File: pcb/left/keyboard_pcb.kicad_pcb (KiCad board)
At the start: 2 copper layers, 138.8 x 89.9 mm, 36 parts, among them J1 TRRS, K00 KEYSW, K01 KEYSW, K02 KEYSW, K03 KEYSW, K04 KEYSW, K05 KEYSW, K10 KEYSW, K11 KEYSW, K12 KEYSW, K13 KEYSW, K14 KEYSW, K15 KEYSW, K20 KEYSW, K21 KEYSW, K22 KEYSW, K23 KEYSW, K24 KEYSW, K25 KEYSW, K30 KEYSW, K31 KEYSW, K32 KEYSW, U2 Pico

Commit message: Fix mounting holes
There were two H1s and three H4s! Add H5–7 and assign M2 mounting hole from KiCad library (no visible change noticed when updating on PCB).
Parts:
- renumbered H4 to H5, H4 to H6, H1 to H7
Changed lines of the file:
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@@
     (property "Sheetname" "")
     (attr exclude_from_pos_files)
-    (fp_text reference "H4" (at 0 -3.2) (layer "F.SilkS") hide
+    (fp_text reference "H5" (at 0 -3.2) (layer "F.SilkS") hide
         (effects (font (size 1 1) (thickness 0.15)))
     )
@@
     (property "Sheetname" "")
     (attr exclude_from_pos_files)
-    (fp_text reference "H4" (at 0 -3.2) (layer "F.SilkS") hide
+    (fp_text reference "H6" (at 0 -3.2) (layer "F.SilkS") hide
         (effects (font (size 1 1) (thickness 0.15)))
     )
@@
     (property "Sheetname" "")
     (attr exclude_from_pos_files)
-    (fp_text reference "H1" (at 0 -3.2) (layer "F.SilkS") hide
-        (effects (font (size 1 1) (thickness 0.15)))
-    )
+    (fp_text reference "H7" (at 0 -3.2) (layer "F.SilkS") hide
+        (effects (font (size 1 1) (thickness 0.15)))
+    )

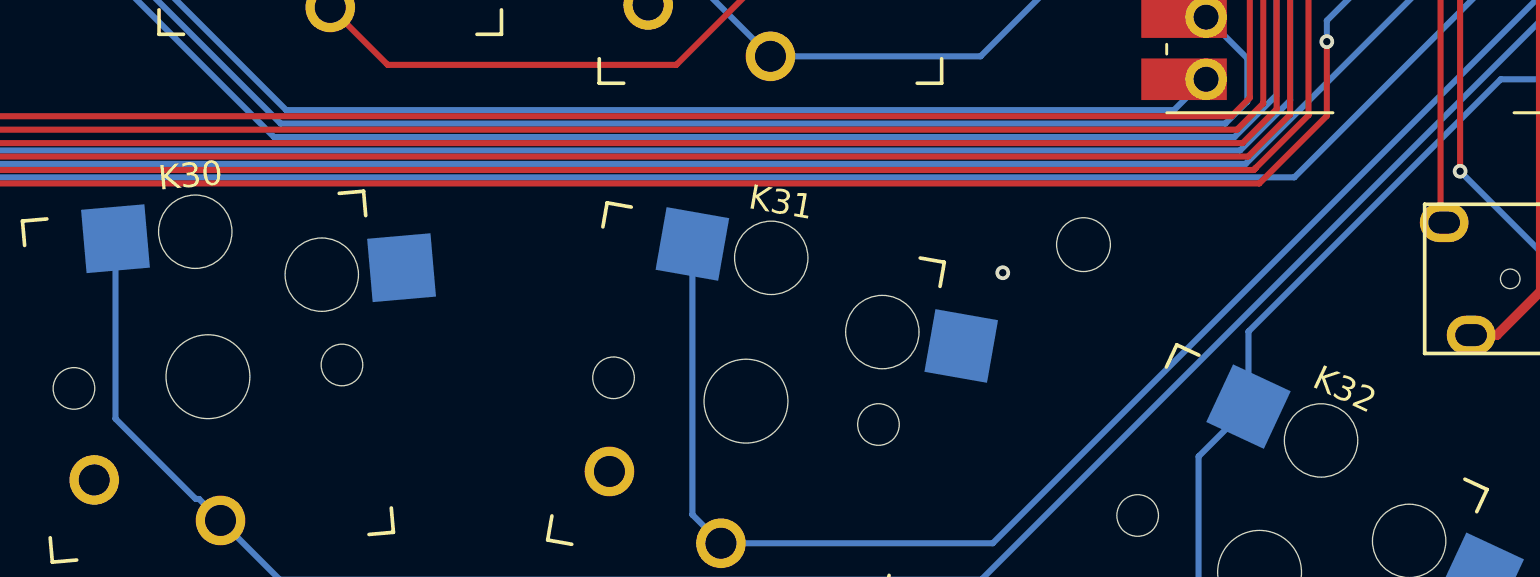
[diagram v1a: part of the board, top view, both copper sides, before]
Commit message: Renumber thumb keys to match new schematic
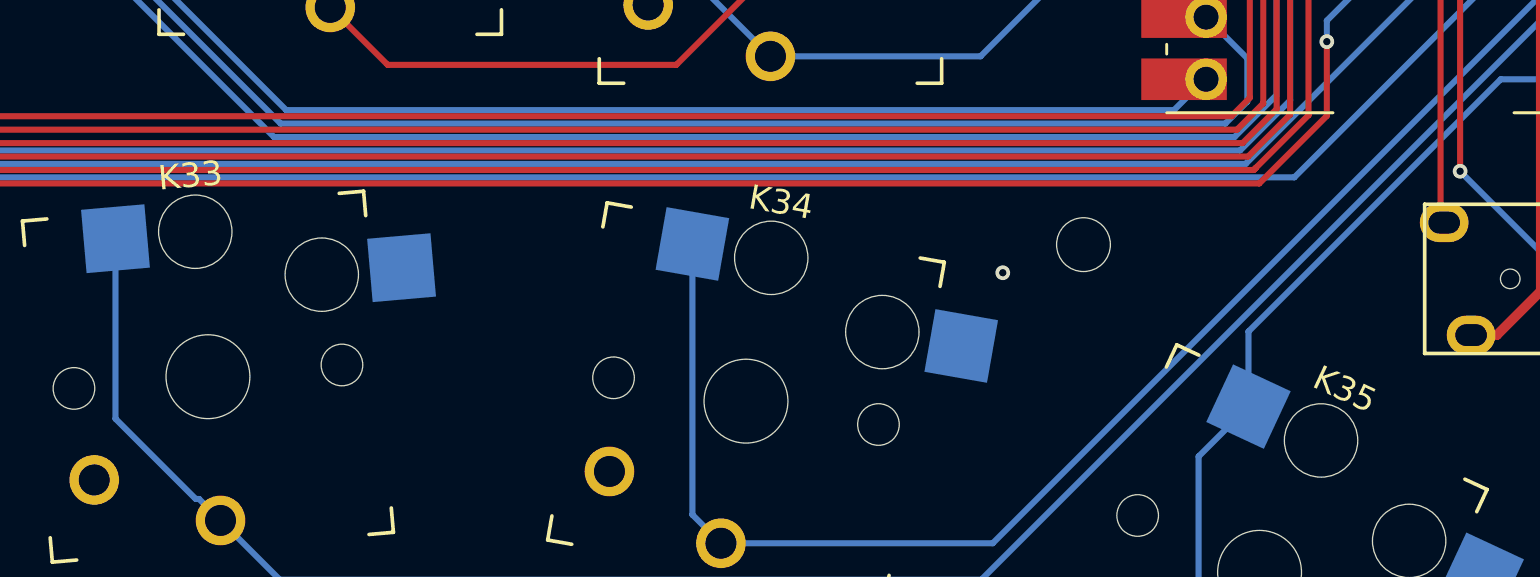
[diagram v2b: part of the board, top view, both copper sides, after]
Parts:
- renumbered K30 to K33, K31 to K34, K32 to K35
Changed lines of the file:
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@@
     (property "Sheetname" "")
     (attr through_hole)
-    (fp_text reference "K30" (at 0 -8.255 5) (layer "F.SilkS")
+    (fp_text reference "K33" (at 0 -8.255 5) (layer "F.SilkS")
         (effects (font (size 1 1) (thickness 0.15)))
     )
@@
     (property "Sheetname" "")
     (attr through_hole)
-    (fp_text reference "K32" (at 0 -8.255 -25) (layer "F.SilkS")
-        (effects (font (size 1 1) (thickness 0.15)))
-    )
-    (fp_text value "KEYSW" (at 0 8.25 -25) (layer "F.Fab")
-        (effects (font (size 1 1) (thickness 0.15)))
-    )
-    (fp_text user "${REFERENCE}" (at 4.445 -7.62 -25) (layer "B.SilkS")
-        (effects (font (size 1 1) (thickness 0.15)) (justify mirror))
-    )
-    (fp_text user "${VALUE}" (at 2.54 -0.635 -25) (layer "B.Fab")
+    (fp_text reference "K35" (at 0 -8.255 155) (layer "F.SilkS")
+        (effects (font (size 1 1) (thickness 0.15)))
+    )
+    (fp_text value "KEYSW" (at 0 8.25 155) (layer "F.Fab")
+        (effects (font (size 1 1) (thickness 0.15)))
+    )
+    (fp_text user "${REFERENCE}" (at 4.445 -7.62 155) (layer "B.SilkS")
+        (effects (font (size 1 1) (thickness 0.15)) (justify mirror))
+    )
+    (fp_text user "${VALUE}" (at 2.54 -0.635 155) (layer "B.Fab")
         (effects (font (size 1 1) (thickness 0.15)) (justify mirror))
     )
@@
         (effects (font (size 1 1) (thickness 0.15)) (justify mirror))
     )
-    (fp_text user "${REFERENCE}" (at 0 0 -25) (layer "F.Fab")
+    (fp_text user "${REFERENCE}" (at 0 0 155) (layer "F.Fab")
         (effects (font (size 1 1) (thickness 0.15)))
     )
@@
     (property "Sheetname" "")
     (attr through_hole)
-    (fp_text reference "K31" (at 0 -8.255 -10) (layer "F.SilkS")
-        (effects (font (size 1 1) (thickness 0.15)))
-    )
-    (fp_text value "KEYSW" (at 0 8.25 -10) (layer "F.Fab")
-        (effects (font (size 1 1) (thickness 0.15)))
-    )
-    (fp_text user "${REFERENCE}" (at 4.445 -7.62 -10) (layer "B.SilkS")
-        (effects (font (size 1 1) (thickness 0.15)) (justify mirror))
-    )
-    (fp_text user "${VALUE}" (at 2.54 -0.635 -10) (layer "B.Fab")
+    (fp_text reference "K34" (at 0 -8.255 170) (layer "F.SilkS")
+        (effects (font (size 1 1) (thickness 0.15)))
+    )
+    (fp_text value "KEYSW" (at 0 8.25 170) (layer "F.Fab")
+        (effects (font (size 1 1) (thickness 0.15)))
+    )
+    (fp_text user "${REFERENCE}" (at 4.445 -7.62 170) (layer "B.SilkS")
+        (effects (font (size 1 1) (thickness 0.15)) (justify mirror))
+    )
+    (fp_text user "${VALUE}" (at 2.54 -0.635 170) (layer "B.Fab")
         (effects (font (size 1 1) (thickness 0.15)) (justify mirror))
     )
@@
         (effects (font (size 1 1) (thickness 0.15)) (justify mirror))
     )
-    (fp_text user "${REFERENCE}" (at 0 0 -10) (layer "F.Fab")
-        (effects (font (size 1 1) (thickness 0.15)))
-    )
+    (fp_text user "${REFERENCE}" (at 0 0 170) (layer "F.Fab")
+        (effects (font (size 1 1) (thickness 0.15)))
+    )

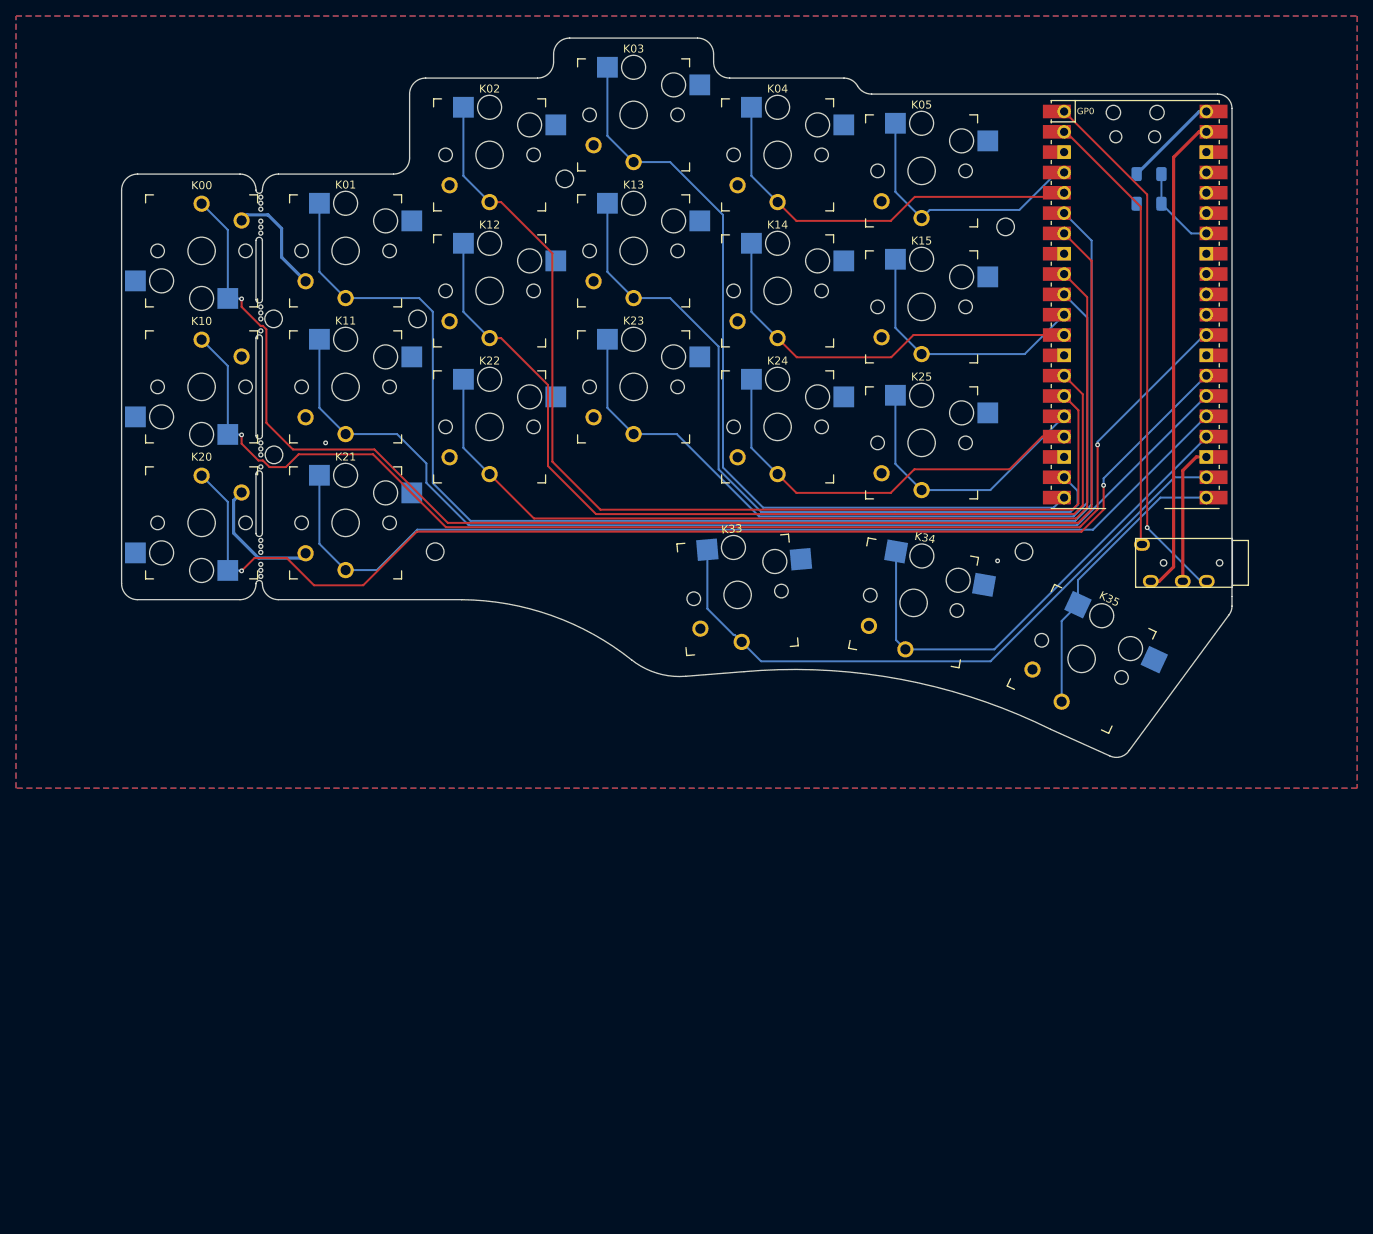
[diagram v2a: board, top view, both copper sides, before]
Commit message: Clean PCB
 * Remove all tracks and vias
 * Remove VBUS detect resistors
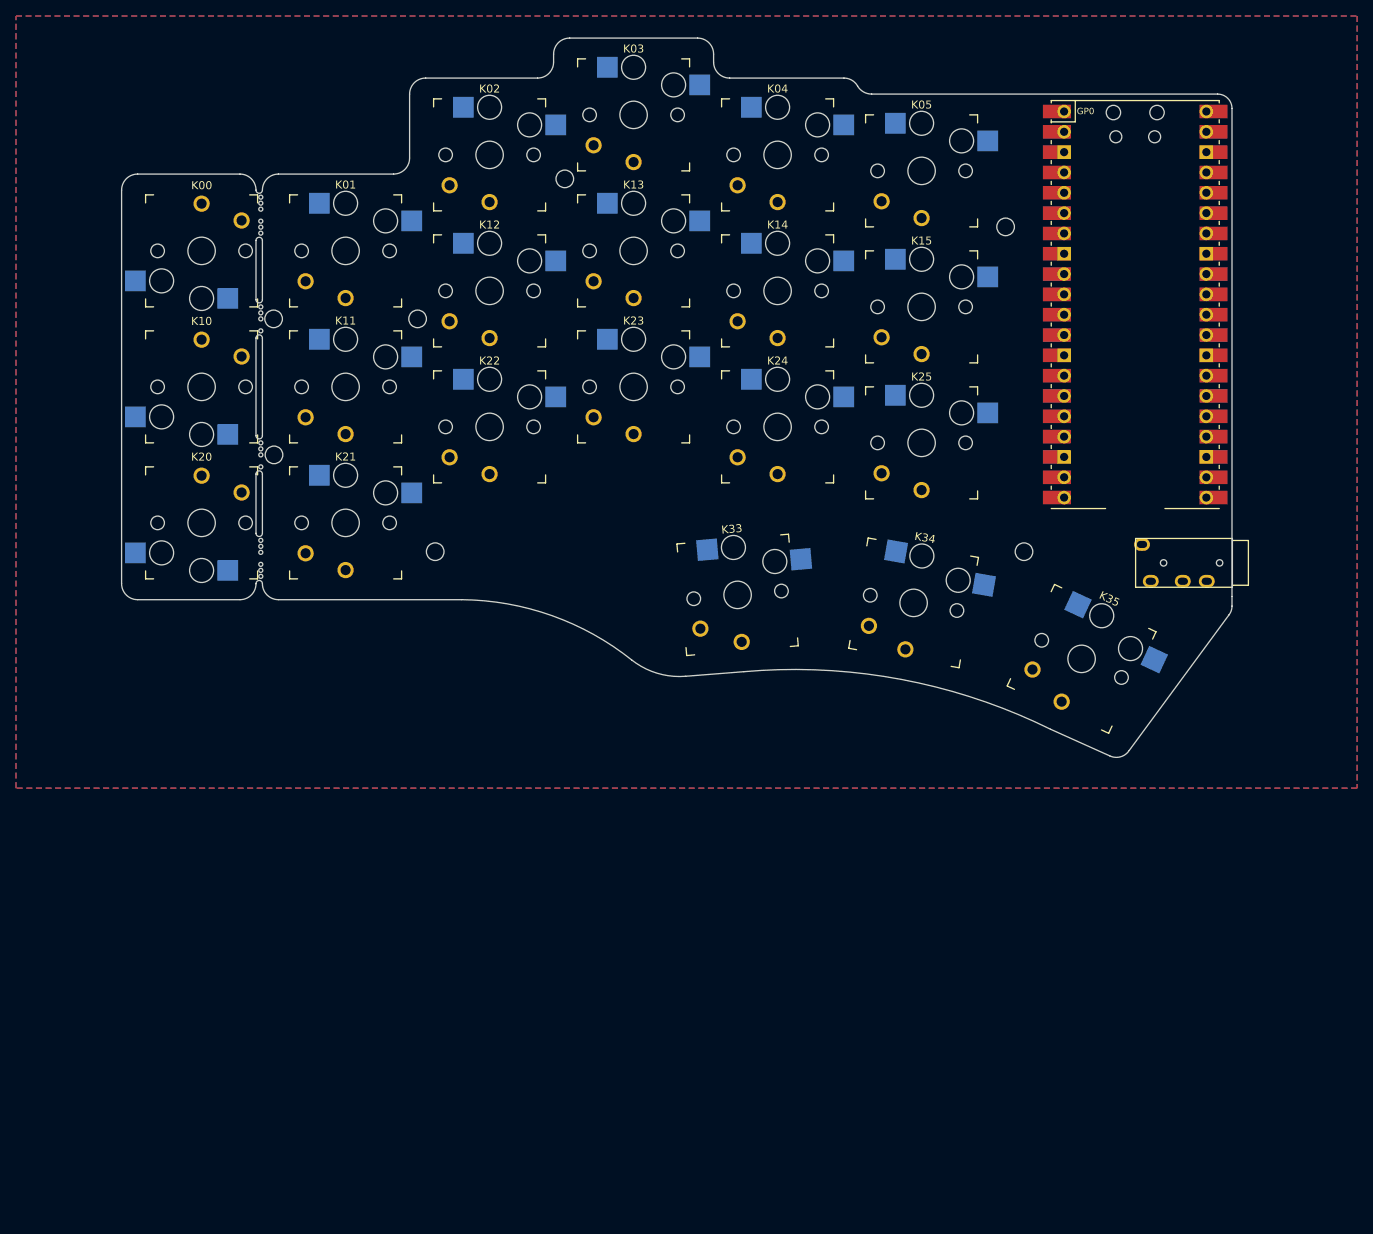
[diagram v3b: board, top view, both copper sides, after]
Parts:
- removed R1: 5k6, Resistor_SMD:R_1206_3216Metric_Pad1.30x1.75mm_HandSolder
- removed R2: 10k, Resistor_SMD:R_1206_3216Metric_Pad1.30x1.75mm_HandSolder
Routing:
- net /k00: track 176.8 -> 0.00 mm, vias 1 -> 0
- net /k01: track 169.2 -> 0.00 mm
- net /k10: track 157.3 -> 0.00 mm, vias 2 -> 0
- net /k20: track 150.8 -> 0.00 mm, vias 2 -> 0
- net /k11: track 133.6 -> 0.00 mm
- net /k02: track 132.5 -> 0.00 mm
- net /k21: track 128.8 -> 0.00 mm
- net /k22: track 121.1 -> 0.00 mm
- net /k12: track 120.1 -> 0.00 mm
- net /k03: track 103.9 -> 0.00 mm
- net /k23: track 102.1 -> 0.00 mm
- net /k13: track 93.2 -> 0.00 mm
- net /k30: track 82.0 -> 0.00 mm
- net tx: track 66.5 -> 0.00 mm, vias 1 -> 0
- net /k31: track 61.4 -> 0.00 mm
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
